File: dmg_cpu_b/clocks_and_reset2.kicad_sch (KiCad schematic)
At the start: 86 parts

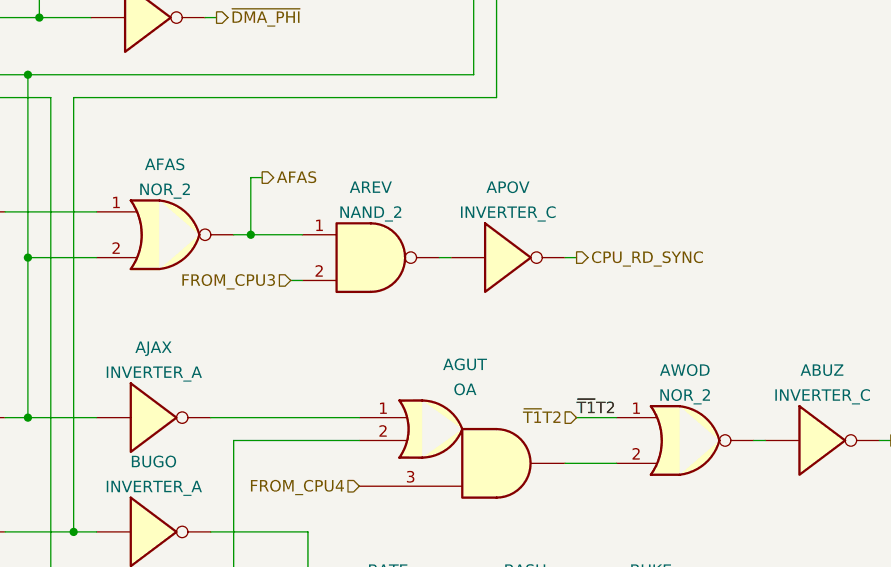
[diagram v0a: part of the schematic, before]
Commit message: addr and data buses added and split on 2 sheets.
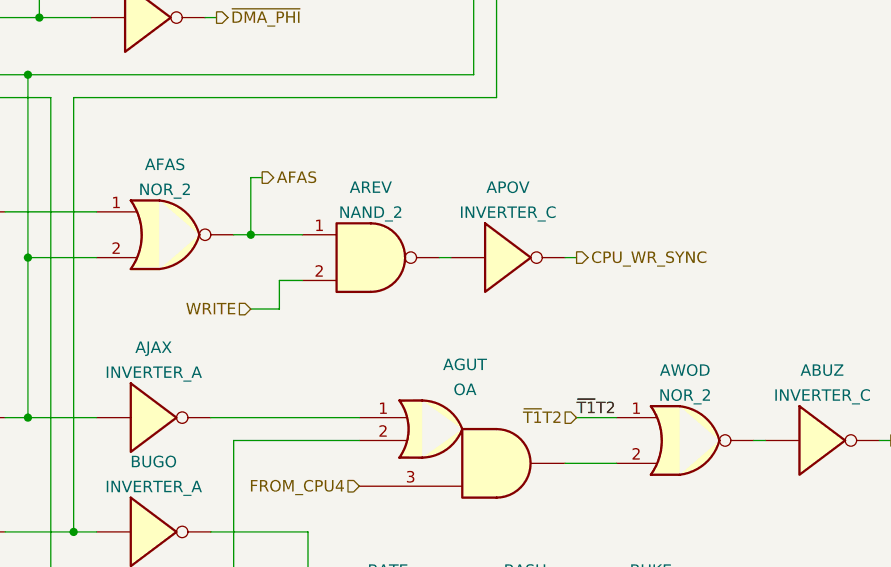
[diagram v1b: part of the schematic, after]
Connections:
- net CPU_RD_SYNC renamed CPU_WR_SYNC
- net FROM_CPU3 renamed WRITE
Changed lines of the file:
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@@
+    (stroke (width 0) (type default) (color 0 0 0 0))
+  )
+  (wire (pts (xy 161.925 108.585) (xy 158.75 108.585))
     (stroke (width 0) (type default) (color 0 0 0 0))
   )
@@
     (stroke (width 0) (type default) (color 0 0 0 0))
   )
-  (wire (pts (xy 163.195 105.41) (xy 164.465 105.41))
+  (wire (pts (xy 161.925 105.41) (xy 164.465 105.41))
     (stroke (width 0) (type default) (color 0 0 0 0))
   )
@@
   )
   (wire (pts (xy 62.23 66.675) (xy 63.5 66.675))
+    (stroke (width 0) (type default) (color 0 0 0 0))
+  )
+  (wire (pts (xy 161.925 108.585) (xy 161.925 105.41))
     (stroke (width 0) (type default) (color 0 0 0 0))
   )
@@
     (effects (font (size 1.27 1.27)) (justify right))
   )
-  (hierarchical_label "FROM_CPU3" (shape input) (at 163.195 105.41 180)
-    (effects (font (size 1.27 1.27)) (justify right))
-  )
   (hierarchical_label "~{RESET6}" (shape output) (at 322.58 156.21 0)
     (effects (font (size 1.27 1.27)) (justify left))
@@
     (effects (font (size 1.27 1.27)) (justify left))
   )
-  (hierarchical_label "CPU_RD_SYNC" (shape output) (at 194.945 102.87 0)
+  (hierarchical_label "CPU_WR_SYNC" (shape output) (at 194.945 102.87 0)
     (effects (font (size 1.27 1.27)) (justify left))
   )
@@
     (effects (font (size 1.27 1.27)) (justify right))
   )
+  (hierarchical_label "WRITE" (shape input) (at 158.75 108.585 180)
+    (effects (font (size 1.27 1.27)) (justify right))
+  )

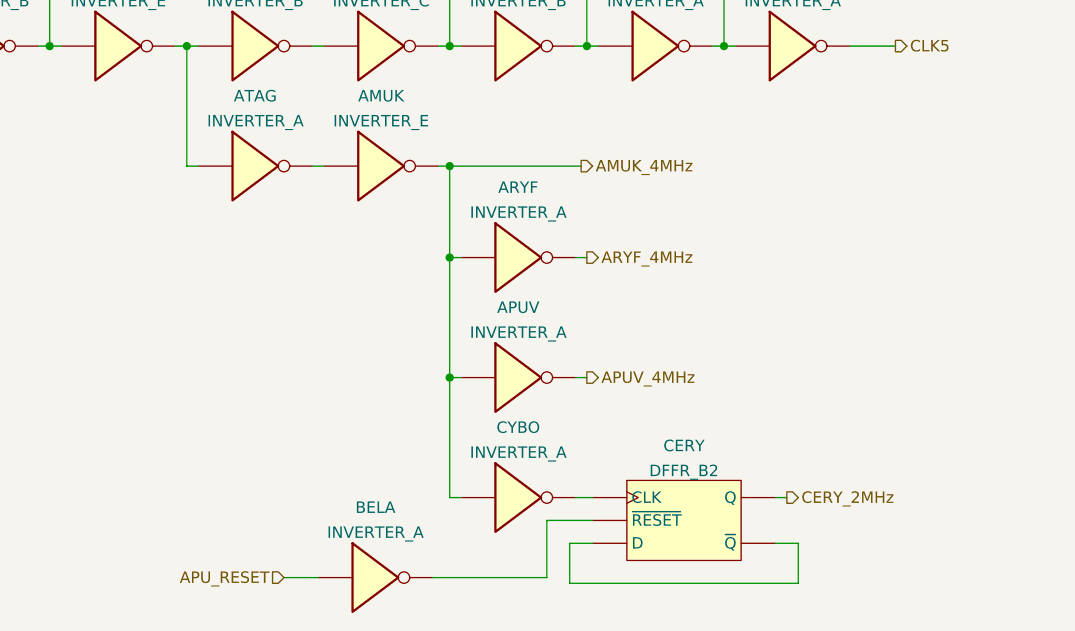
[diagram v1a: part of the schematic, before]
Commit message: APU started: control regs, APU address decoding.
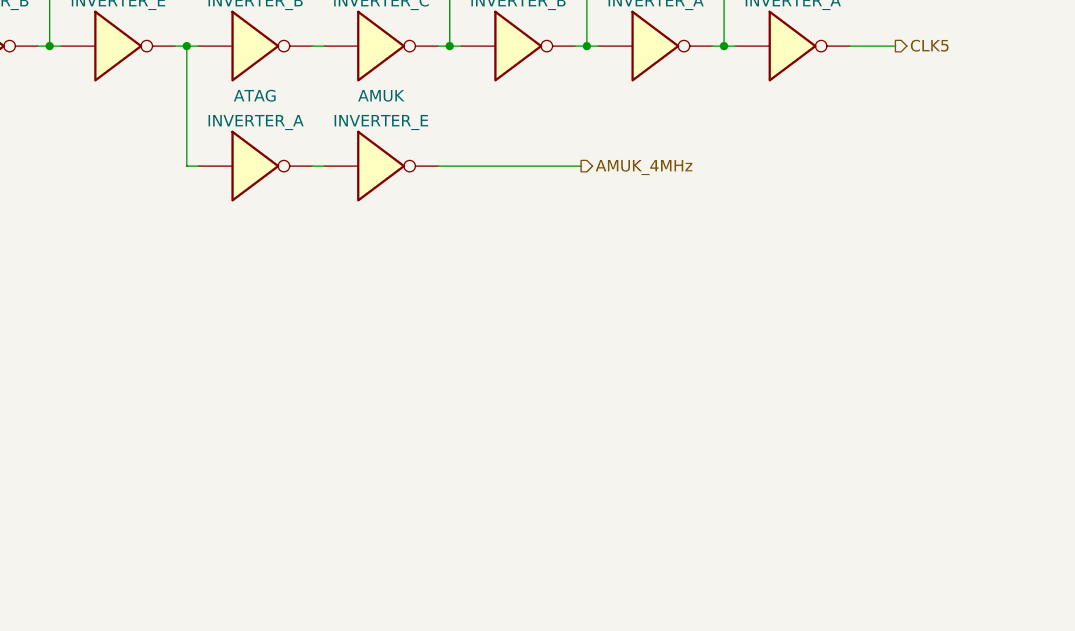
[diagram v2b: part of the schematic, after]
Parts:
- removed APUV, ARYF, BELA, CYBO: INVERTER_A, symbol DMG_CPU_Cells:INVERTER_A
- removed CERY: DFFR_B2, symbol DMG_CPU_Cells:DFFR_B2

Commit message: First lot of fixes based on issues found.
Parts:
- added PHI: OBUF_A, symbol DMG_CPU_Cells:OBUF_A
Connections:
- net RESET: now also ASOL.4 (RESET); no longer ASOL.1 (SET)
- net at AGUT.1: now also AROV.2, BAPY.2, BATE.2; no longer AJAX.2
- net at BAVY.1, BEKO.1, BEVA.2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: now also PHI.1 (~{OUTPUT})
- net at ASOL.2 (~{Q}): now also AFER.2 (D), AVOR.2
- net at AFAR.3: now also ASOL.1 (SET); no longer ASOL.4 (RESET)
- new net: AGUT.2, AJAX.2
- now unconnected: ASOL.3 (Q)
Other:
- moved on the sheet: ABUZ, ADAR, ADYK, AFAR, AFAS, AFEP, AFUR, AGUT, AJAX, ALEF, ALET, ALYP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

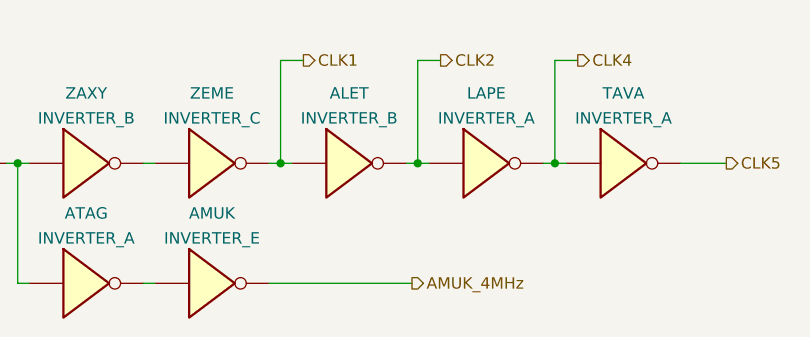
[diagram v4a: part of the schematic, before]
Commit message: Fixes made from issues, channel 4 sheet aded and tidy up of hierarchical APU sheet. Small fixes done here and there when doing ERC.
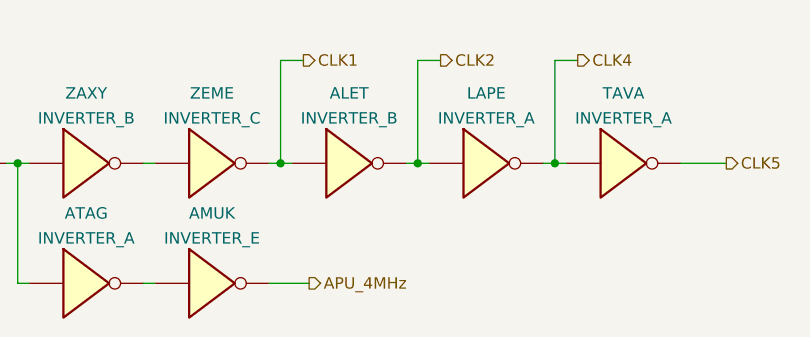
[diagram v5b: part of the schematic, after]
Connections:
- net AMUK_4MHz renamed APU_4MHz
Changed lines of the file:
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@@
     (stroke (width 0) (type default) (color 0 0 0 0))
   )
-  (wire (pts (xy 154.94 260.35) (xy 170.815 260.35))
+  (wire (pts (xy 154.94 260.35) (xy 159.385 260.35))
     (stroke (width 0) (type default) (color 0 0 0 0))
   )
@@
     (effects (font (size 1.27 1.27)) (justify right))
   )
-  (hierarchical_label "AMUK_4MHz" (shape output) (at 170.815 260.35 0)
-    (effects (font (size 1.27 1.27)) (justify left))
-  )
+  (hierarchical_label "APU_4MHz" (shape output) (at 159.385 260.35 0)
+    (effects (font (size 1.27 1.27)) (justify left))
+  )

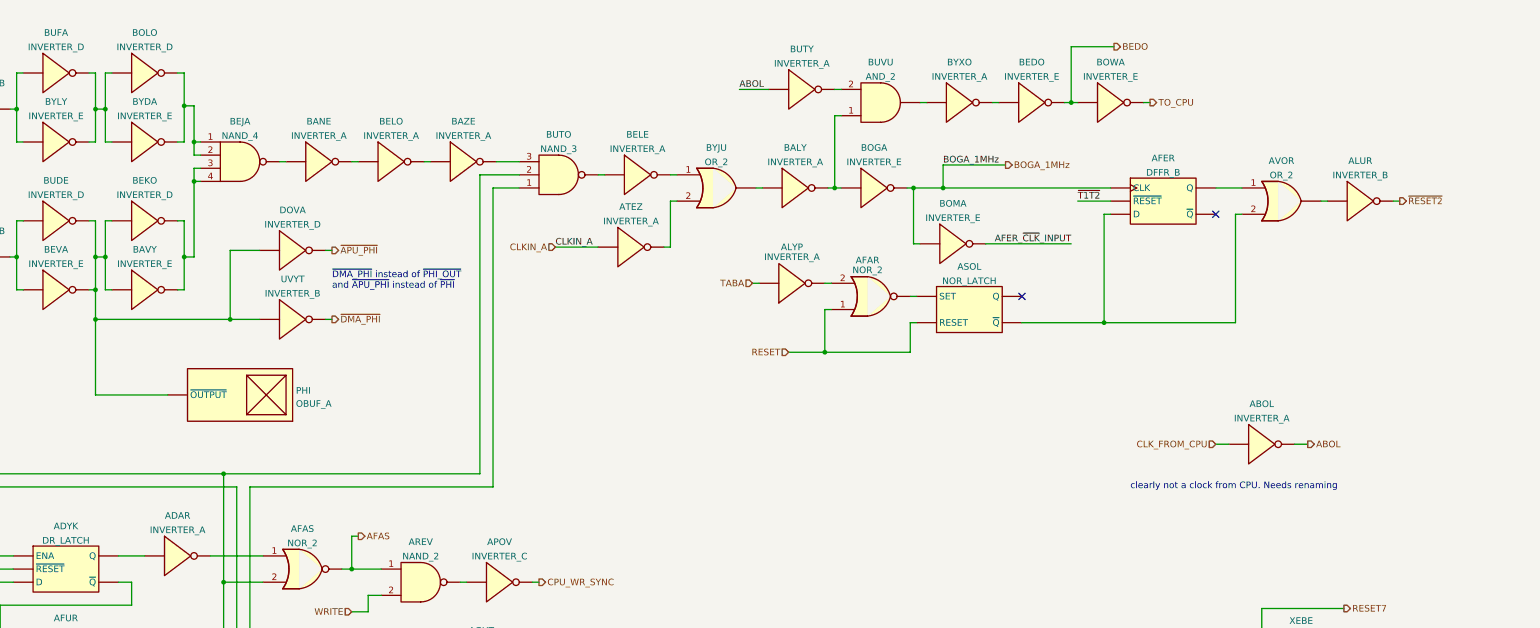
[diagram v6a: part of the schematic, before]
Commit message: Fixes made based on raised issues. PPU decode page added as draft level.
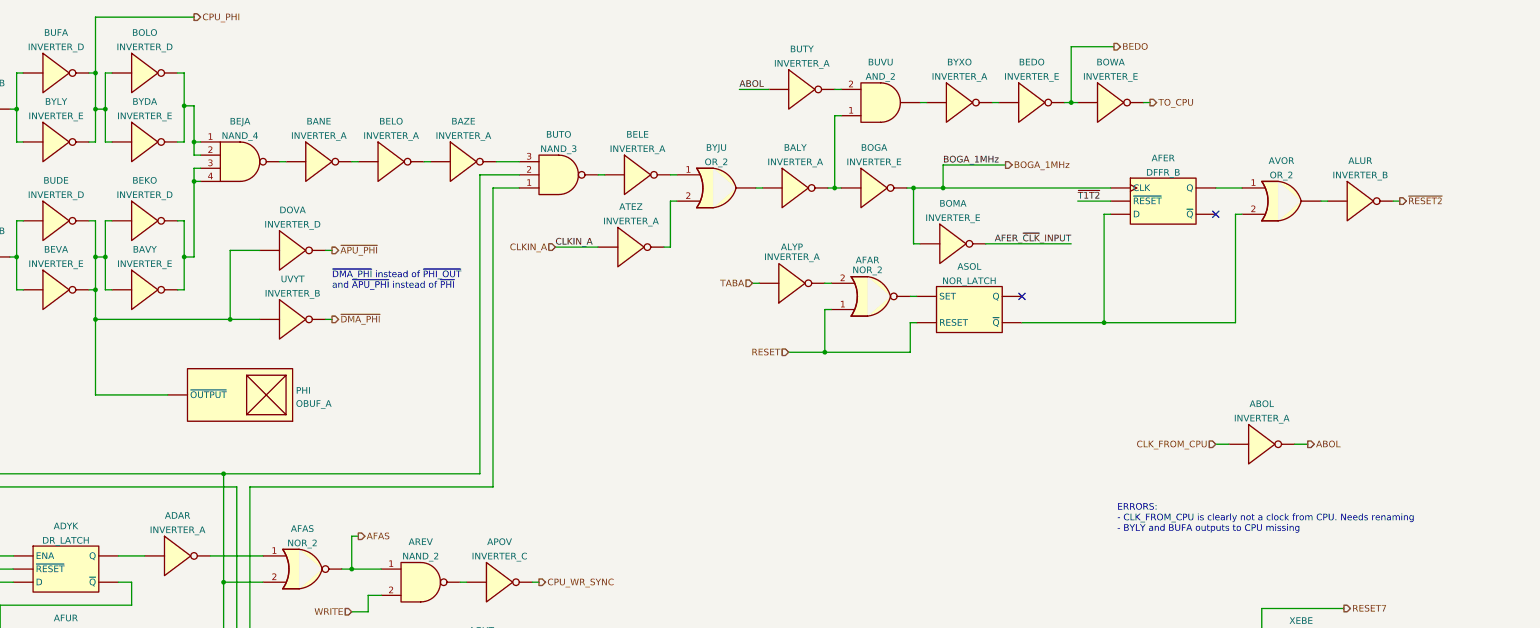
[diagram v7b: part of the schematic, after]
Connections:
- net CPU_PHI: now reaches BOLO.1, BUFA.2, BYDA.1, BYLY.2
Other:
- note added: "ERRORS: - CLK_FROM_CPU is clearly not a clock from CPU. Needs renaming - BYLY and BUFA outputs to CPU missing"
- note removed: "clearly not a clock from CPU. Needs renaming"
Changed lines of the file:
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@@
   (junction (at 85.725 160.02) (diameter 0) (color 0 0 0 0)
+  )
+  (junction (at 109.22 28.575) (diameter 0) (color 0 0 0 0)
   )
   (junction (at 158.75 124.46) (diameter 0) (color 0 0 0 0)
@@
     (stroke (width 0) (type default) (color 0 0 0 0))
   )
+  (wire (pts (xy 109.22 28.575) (xy 109.22 17.78))
+    (stroke (width 0) (type default) (color 0 0 0 0))
+  )
   (wire (pts (xy 267.335 50.8) (xy 273.05 50.8))
     (stroke (width 0) (type default) (color 0 0 0 0))
@@
   )
   (wire (pts (xy 109.22 64.135) (xy 111.125 64.135))
+    (stroke (width 0) (type default) (color 0 0 0 0))
+  )
+  (wire (pts (xy 109.22 17.78) (xy 128.27 17.78))
     (stroke (width 0) (type default) (color 0 0 0 0))
   )
@@
     (effects (font (size 1.27 1.27)) (justify left bottom))
   )
-  (text "clearly not a clock from CPU. Needs renaming" (at 309.245 109.22 0)
+  (text "ERRORS:\n- CLK_FROM_CPU is clearly not a clock from CPU. Needs renaming\n- BYLY and BUFA outputs to CPU missing"
+    (at 306.705 117.475 0)
     (effects (font (size 1.27 1.27)) (justify left bottom))
   )
@@
     (effects (font (size 1.27 1.27)) (justify left))
   )
+  (hierarchical_label "CPU_PHI" (shape output) (at 128.27 17.78 0)
+    (effects (font (size 1.27 1.27)) (justify left))
+  )

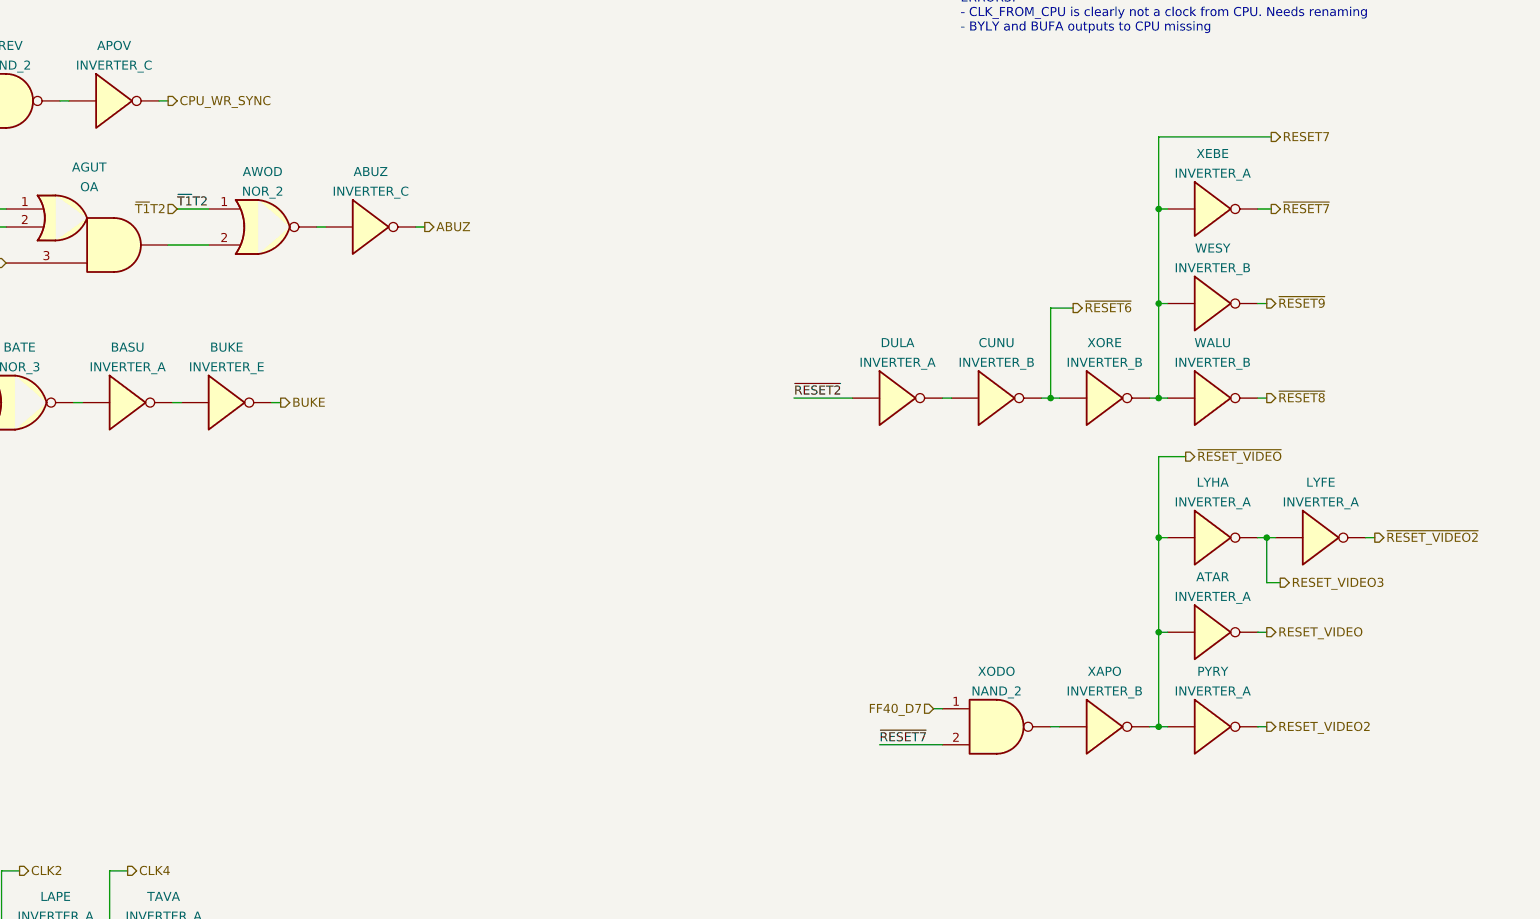
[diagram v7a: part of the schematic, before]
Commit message: FF40,41,44,45 regs and LCD added
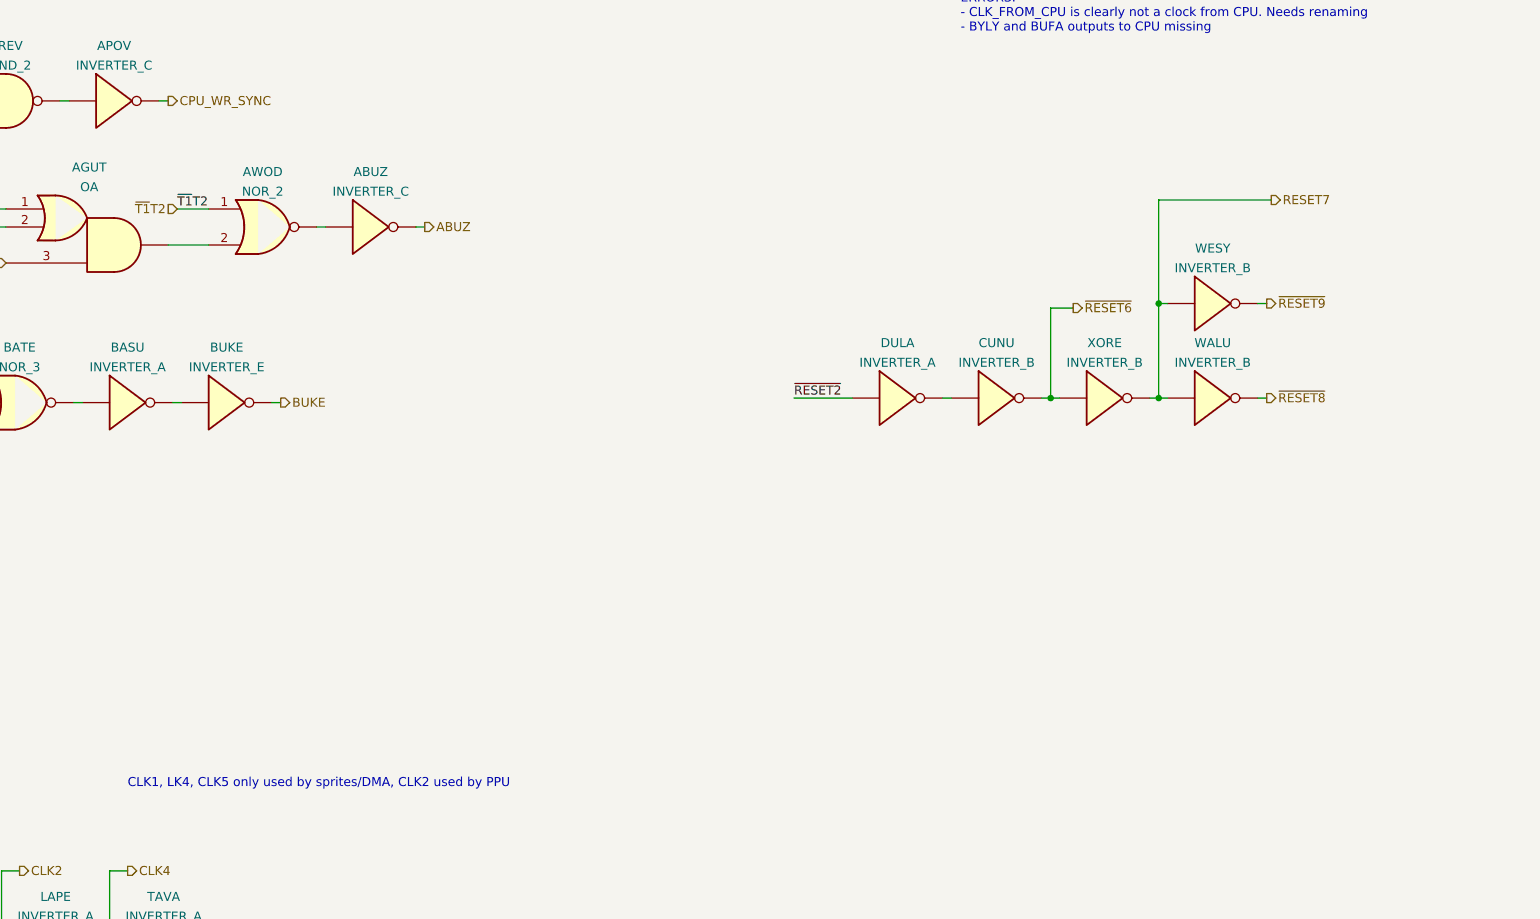
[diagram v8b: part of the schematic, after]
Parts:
- removed ATAR, LYFE, LYHA, PYRY, XEBE: INVERTER_A, symbol DMG_CPU_Cells:INVERTER_A
- removed XAPO: INVERTER_B, symbol DMG_CPU_Cells:INVERTER_B
- removed XODO: NAND_2, symbol DMG_CPU_Cells:NAND_2
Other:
- note added: "CLK1, LK4, CLK5 only used by sprites/DMA, CLK2 used by PPU"
